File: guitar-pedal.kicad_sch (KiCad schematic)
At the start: 53 parts, among them J1 USB_OTG, J2 AudioJack2, J3 AudioJack2, J4 Test_Headers, SW1 SW_SPST, SW2 SW_3PDT, SW3 Boot, SW3 SW_Push_SPDT, SW4 Reset, SW4 SW_Push_SPDT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

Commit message: create ES8374 codec symbol
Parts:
- removed SW1: SW_SPST, symbol Switch:SW_SPST
- added SW1: SW_SPDT, symbol Switch:SW_SPDT
- renumbered SW3 to SW5, SW4 to SW6
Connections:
- net +5V: now also SW1.1 (A)
- net at J1.1 (VBUS): now also SW1.2 (B)
- no-connect marks 18 -> 19
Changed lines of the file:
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@@
   (junction (at 96.266 122.174) (diameter 0) (color 0 0 0 0)
   )
+  (junction (at 37.338 39.624) (diameter 0) (color 0 0 0 0)
+  )
   (junction (at 248.666 103.632) (diameter 0) (color 0 0 0 0)
   )
@@
   )
   (junction (at 29.718 54.864) (diameter 0) (color 0 0 0 0)
-  )
-  (junction (at 37.338 39.624) (diameter 0) (color 0 0 0 0)
   )
   (junction (at 266.7 105.918) (diameter 0) (color 0 0 0 0)
@@
   (no_connect (at 355.6 176.784))
   (no_connect (at 355.6 161.544))
+  (no_connect (at 47.498 42.164))
   (wire (pts (xy 269.24 153.924) (xy 242.57 153.924))
     (stroke (width 0) (type default) (color 0 0 0 0))
@@
     (stroke (width 0) (type default) (color 0 0 0 0))
   )
-  (wire (pts (xy 47.498 32.258) (xy 47.498 39.624))
-    (stroke (width 0) (type default) (color 0 0 0 0))
-  )
   (wire (pts (xy 52.324 115.062) (xy 92.456 115.062))
     (stroke (width 0) (type default) (color 0 0 0 0))
@@
   )
   (polyline (pts (xy 327.66 75.692) (xy 378.46 75.692))
+    (stroke (width 0) (type default) (color 0 0 0 0))
+  )
+  (wire (pts (xy 47.498 32.258) (xy 47.498 37.084))
     (stroke (width 0) (type default) (color 0 0 0 0))
   )
@@
     )
     (property "Datasheet" "~" (id 3) (at 271.78 100.838 0)
-      (effects (font (size 1.27 1.27)) hide)
-    )
-    (pin "1")
-    (pin "2")
-  )
-  (symbol (lib_id "Switch:SW_SPST") (at 42.418 39.624 0) (unit 1)
-    (in_bom yes) (on_board yes)
-    (property "Reference" "SW1" (id 0) (at 42.418 34.036 0))
-    (property "Value" "SW_SPST" (id 1) (at 42.418 36.322 0))
-    (property "Footprint" "" (id 2) (at 42.418 39.624 0)
-      (effects (font (size 1.27 1.27)) hide)
-    )
-    (property "Datasheet" "~" (id 3) (at 42.418 39.624 0)
       (effects (font (size 1.27 1.27)) hide)
     )
@@
   (symbol (lib_id "Switch:SW_Push_SPDT") (at 225.044 187.198 0) (mirror y) (unit 1)
     (in_bom yes) (on_board yes)
-    (property "Reference" "SW4" (id 0) (at 225.044 192.278 0))
+    (property "Reference" "SW6" (id 0) (at 225.044 192.278 0))
     (property "Value" "SW_Push_SPDT" (id 1) (at 225.044 194.818 0))
     (property "Footprint" "" (id 2) (at 225.044 187.198 0)
@@
     (pin "1")
   )
+  (symbol (lib_id "Switch:SW_SPDT") (at 42.418 39.624 0) (unit 1)
+    (in_bom yes) (on_board yes) (fields_autoplaced)
+    (property "Reference" "SW1" (id 0) (at 42.418 32.004 0))
+    (property "Value" "SW_SPDT" (id 1) (at 42.418 34.544 0))
+    (property "Footprint" "" (id 2) (at 42.418 39.624 0)
+      (effects (font (size 1.27 1.27)) hide)
+    )
+    (property "Datasheet" "~" (id 3) (at 42.418 39.624 0)
+      (effects (font (size 1.27 1.27)) hide)
+    )
+    (pin "1")
+    (pin "2")
+    (pin "3")
+  )
   (symbol (lib_id "Device:C_Small") (at 97.79 41.91 270) (mirror x) (unit 1)
     (in_bom yes) (on_board yes) (fields_autoplaced)
@@
   )
   (symbol (lib_id "Switch:SW_Push_SPDT") (at 225.044 177.038 0) (mirror y) (unit 1)
-    (in_bom yes) (on_board yes) (fields_autoplaced)
-    (property "Reference" "SW3" (id 0) (at 225.044 169.418 0))
-    (property "Value" "SW_Push_SPDT" (id 1) (at 225.044 171.958 0))
+    (in_bom yes) (on_board yes)
+    (property "Reference" "SW5" (id 0) (at 225.044 169.418 0))
+    (property "Value" "SW_Push_SPDT" (id 1) (at 225.044 171.45 0))
     (property "Footprint" "" (id 2) (at 225.044 177.038 0)
       (effects (font (size 1.27 1.27)) hide)
@@
       (reference "R9") (unit 1) (value "165R") (footprint "")
     )
-    (path "/0a7d1484-a322-4193-82a2-3065b70dcfd5"
-      (reference "SW1") (unit 1) (value "SW_SPST") (footprint "")
+    (path "/732faad5-34d1-47ba-b609-95eece767e8b"
+      (reference "SW1") (unit 1) (value "SW_SPDT") (footprint "")
     )
     (path "/6da2e811-c5e0-40c6-9fcd-4ef2253b5fc9"
@@
       (reference "SW3") (unit 1) (value "Boot") (footprint "")
     )
-    (path "/b5893086-0f09-43f7-b584-119c5dd43e8f"
-      (reference "SW3") (unit 1) (value "SW_Push_SPDT") (footprint "")
-    )
     (path "/0340a396-8850-47cb-8e38-907102103ba7"
       (reference "SW4") (unit 1) (value "Reset") (footprint "")
     )
+    (path "/b5893086-0f09-43f7-b584-119c5dd43e8f"
+      (reference "SW5") (unit 1) (value "SW_Push_SPDT") (footprint "")
+    )
     (path "/5175ddde-eefb-4d7b-a15f-ca142556b63a"
-      (reference "SW4") (unit 1) (value "SW_Push_SPDT") (footprint "")
+      (reference "SW6") (unit 1) (value "SW_Push_SPDT") (footprint "")
     )
     (path "/97a20e5d-a5cf-4571-8f05-92697c515df1"

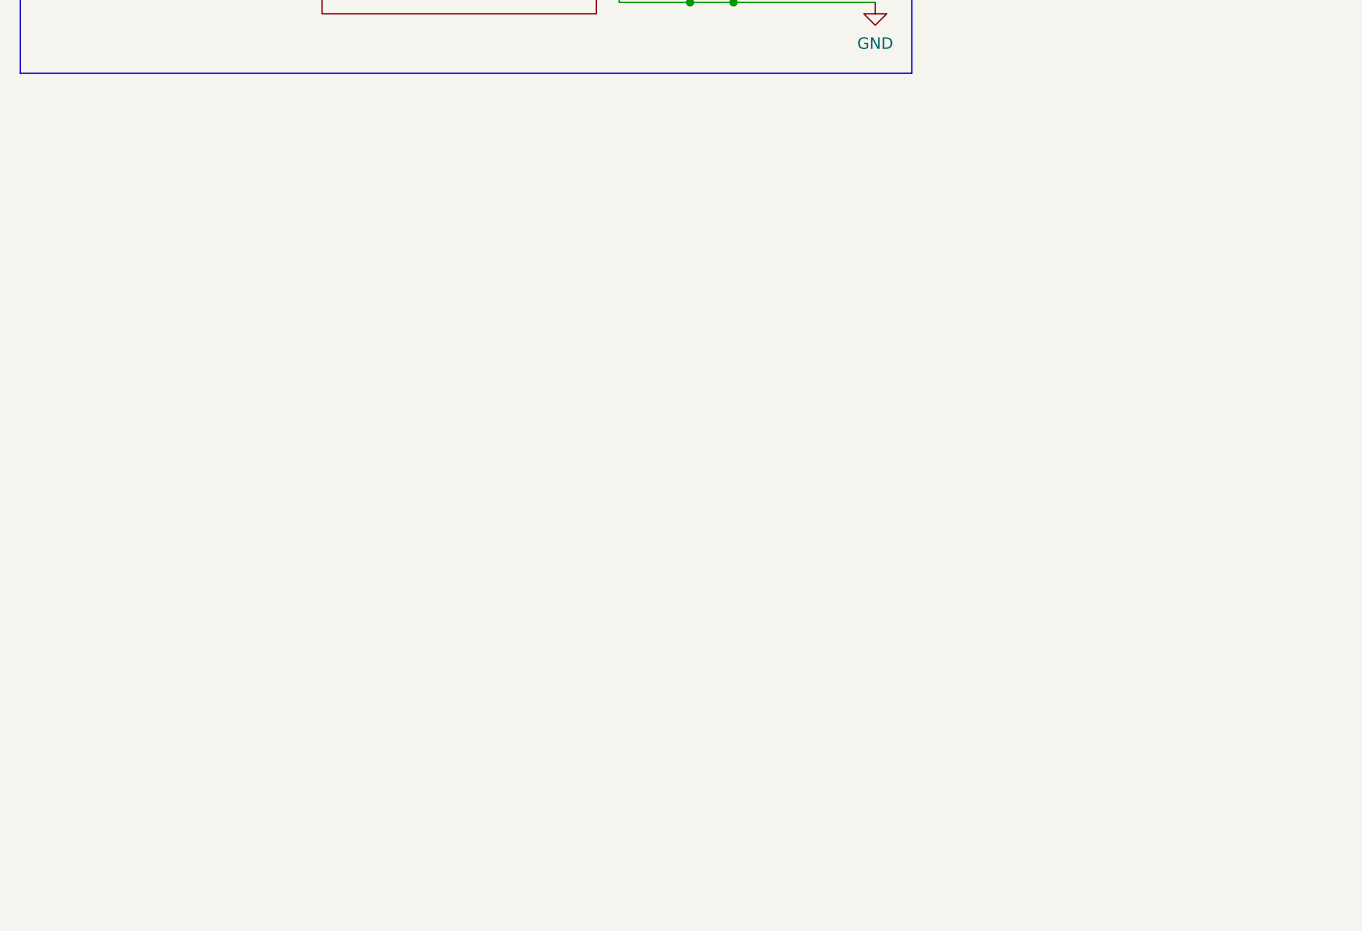
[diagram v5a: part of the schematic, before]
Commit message: add ES8374 codec to schematic and start wiring its pins
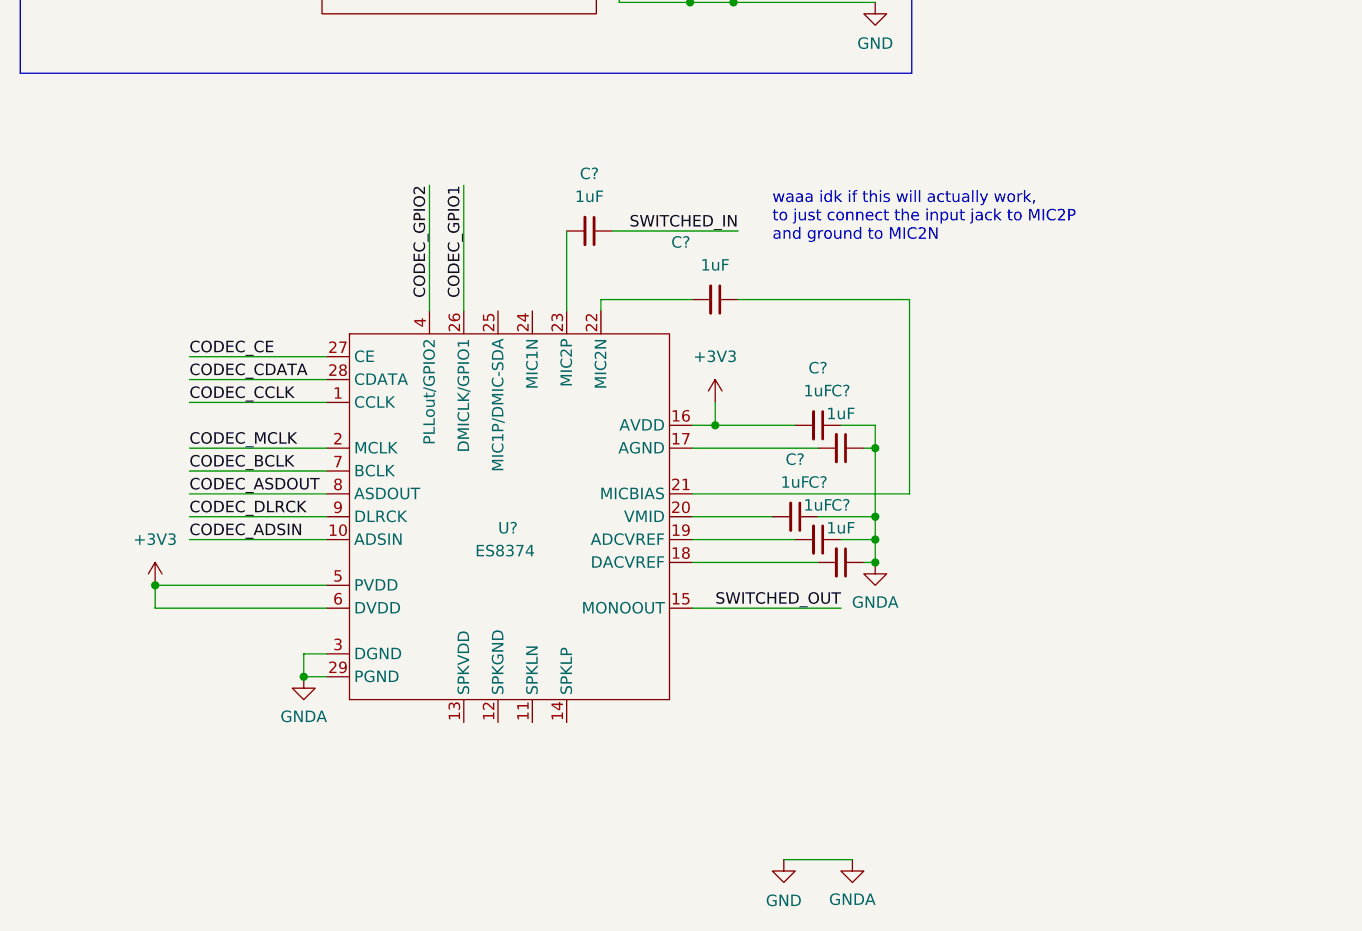
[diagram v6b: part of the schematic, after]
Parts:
- added C? (x7): 1uF, symbol Device:C_Small
- added U?: ES8374, symbol Audio:ES8374
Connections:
- net +3V3: now also C?.2, U?.16 (AVDD), U?.5 (PVDD), U?.6 (DVDD)
- net GND: now also C?.1, C?.1, C?.1, C?.1, C?.1, U?.29 (PGND), U?.3 (DGND)
- net SWITCHED_IN: now also C?.1
- net SWITCHED_OUT: now also U?.15 (MONOOUT)
- new net: C?.2, U?.20 (VMID)
- new net: C?.2, U?.17 (AGND)
- new net: C?.2, U?.23 (MIC2P)
- new net: C?.1, U?.21 (MICBIAS)
- new net: C?.2, U?.22 (MIC2N)
- new net: C?.2, U?.18 (DACVREF)
- new net: C?.2, U?.19 (ADCVREF)
- new net CODEC_ADSIN: U?.10 (ADSIN)
- new net CODEC_ASDOUT: U?.8 (ASDOUT)
- new net CODEC_BCLK: U?.7 (BCLK)
- new net CODEC_CCLK: U?.1 (CCLK)
- new net CODEC_CDATA: U?.28 (CDATA)
- new net CODEC_CE: U?.27 (CE)
- new net CODEC_DLRCK: U?.9 (DLRCK)
- new net CODEC_GPIO1: U?.26 (DMICLK/GPIO1)
- new net CODEC_GPIO2: U?.4 (PLLout/GPIO2)
- new net CODEC_MCLK: U?.2 (MCLK)
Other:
- note added: "waaa idk if this will actually work, to just connect the input jack to MIC2P and ground to MIC2N"

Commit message: poop
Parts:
- added R? (x2): 1M, symbol Device:R_Small_US
- added U?: Opamp_Dual, symbol Device:Opamp_Dual
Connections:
- net +3V3: now also C12.1, C15.1, R?.1
- net BIASED_IN: now also U?.1, U?.2 (-)
- net SWITCHED_IN: now also R?.2
- new net: R?.1, R?.2, U?.3 (+)

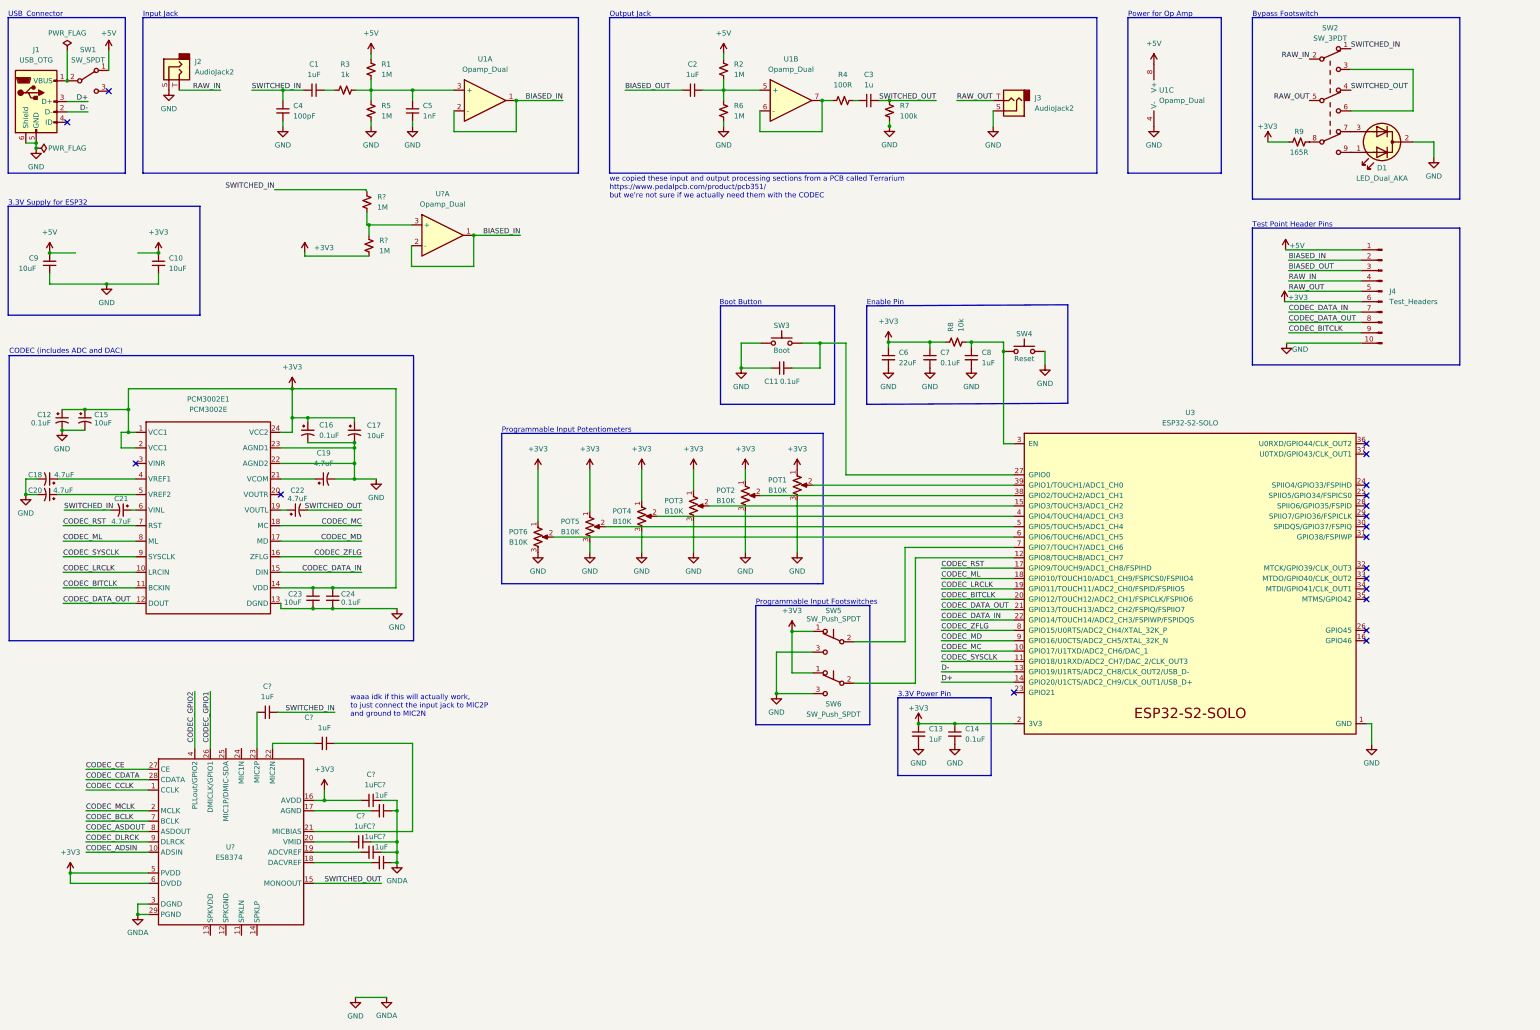
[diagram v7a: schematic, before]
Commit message: figured out pre-and post processing (mostly) and removed ES8374 codec to go back to just PCM3002
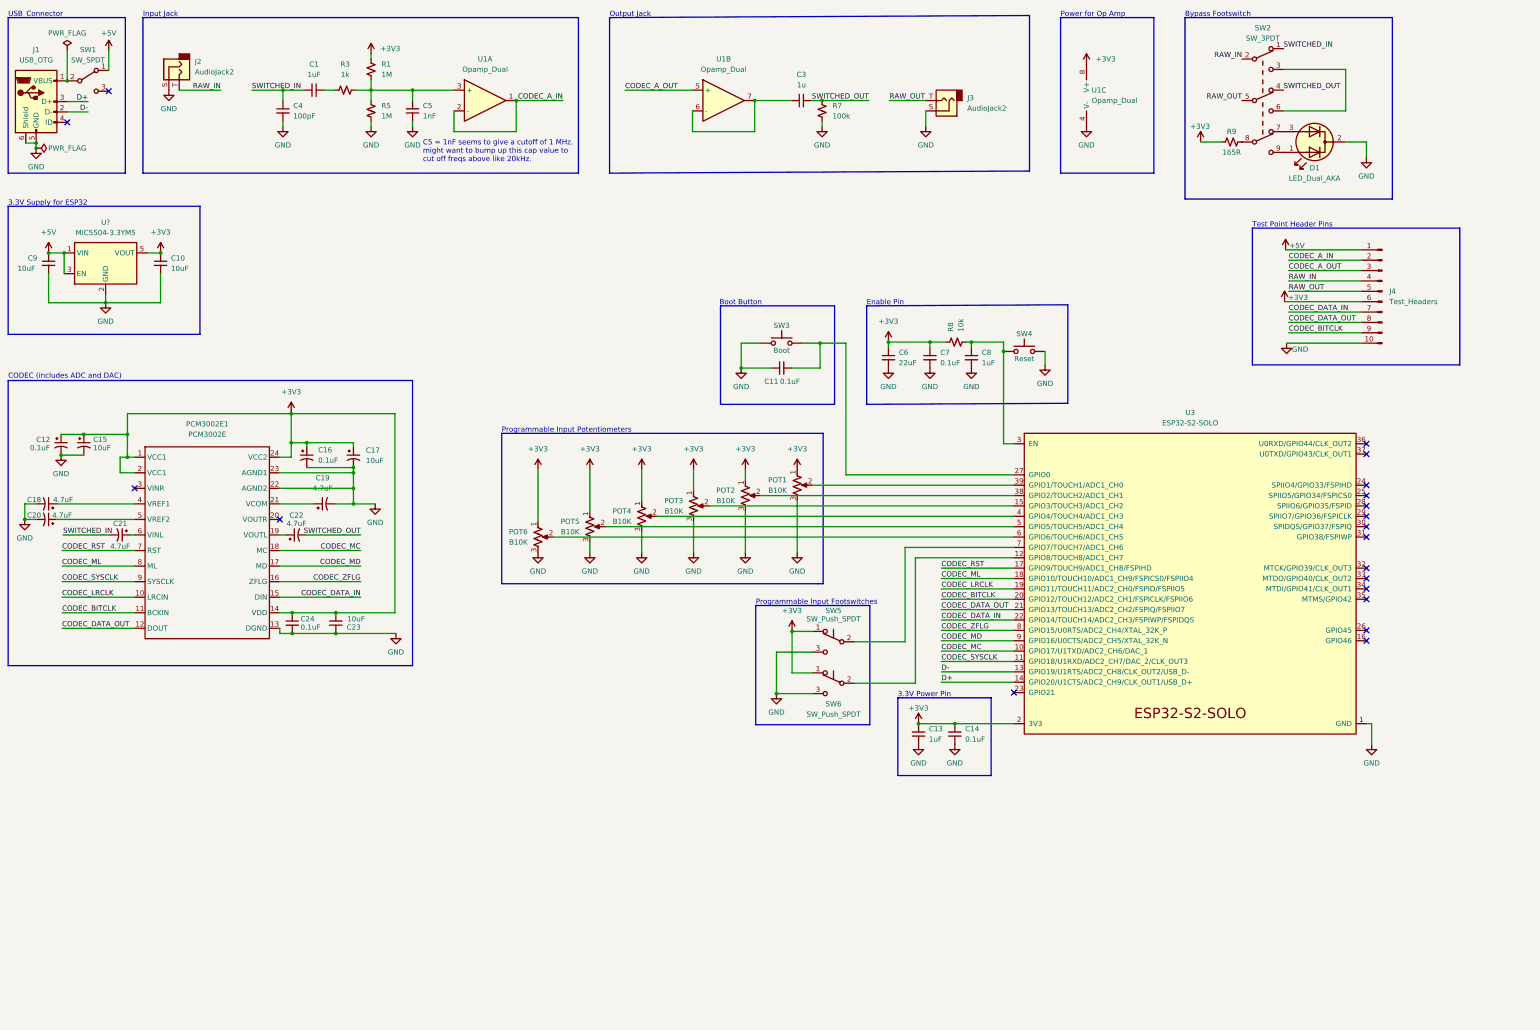
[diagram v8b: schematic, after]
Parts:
- removed C2, C? (x7): 1uF, symbol Device:C_Small
- removed R2, R6, R? (x2): 1M, symbol Device:R_Small_US
- removed R4: 100R, symbol Device:R_Small_US
- removed U?: Opamp_Dual, symbol Device:Opamp_Dual
- removed U?: ES8374, symbol Audio:ES8374
- added U?: MIC5504-3.3YM5, Package_TO_SOT_SMD:SOT-23-5, symbol Regulator_Linear:MIC5504-3.3YM5
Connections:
- net BIASED_OUT is gone; now on net CODEC_A_OUT: J4.3 (Pin_3)
- net +3V3: now also C23.2, R1.2, U1.8 (V+), U?.5 (VOUT); no longer C23.1
- net +5V: now also U?.1 (VIN), U?.3 (EN); no longer R1.2, U1.8 (V+)
- net GND: now also C23.1, U?.2 (GND); no longer C23.2
- net CODEC_A_OUT: now reaches U1.5 (+)
- net at C3.1: now also U1.6 (-), U1.7
- net BIASED_IN renamed CODEC_A_IN
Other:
- note added: "C5 = 1nF seems to give a cutoff of 1 MHz. might want to bump up this cap value to cut off freqs above like 20kHz."
- note removed: "waaa idk if this will actually work, to just connect the input jack to MIC2P and ground to MIC2N"
- note removed: "we copied these input and output processing sections from a PCB called Terrarium https://www.pedalpcb.com/product/pcb351/ but we're not sure if we actually need them with the CODEC"
- moved on the sheet: C10, C12, C15, C16, C17, C18, C19, C20, C21, C22, C23, C24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
